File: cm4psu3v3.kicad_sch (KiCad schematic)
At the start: 26 parts, among them U13 AP64501SP-13

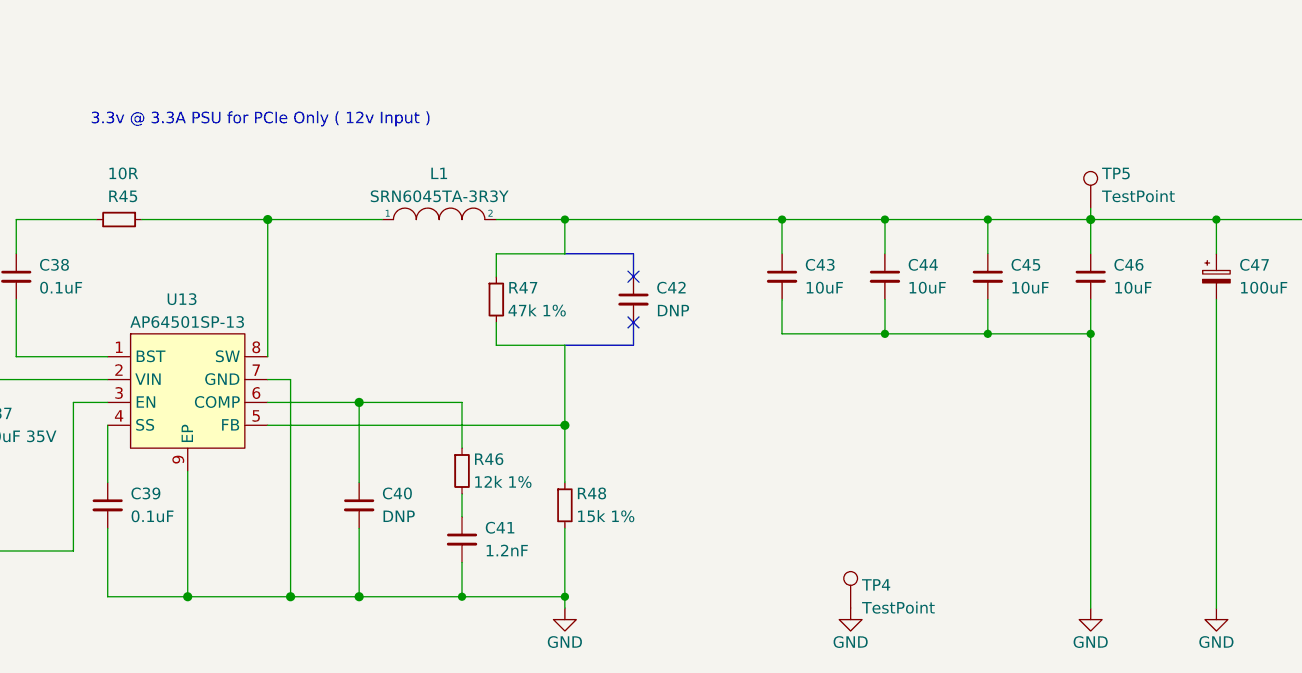
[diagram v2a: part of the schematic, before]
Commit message: added ti buffer lib
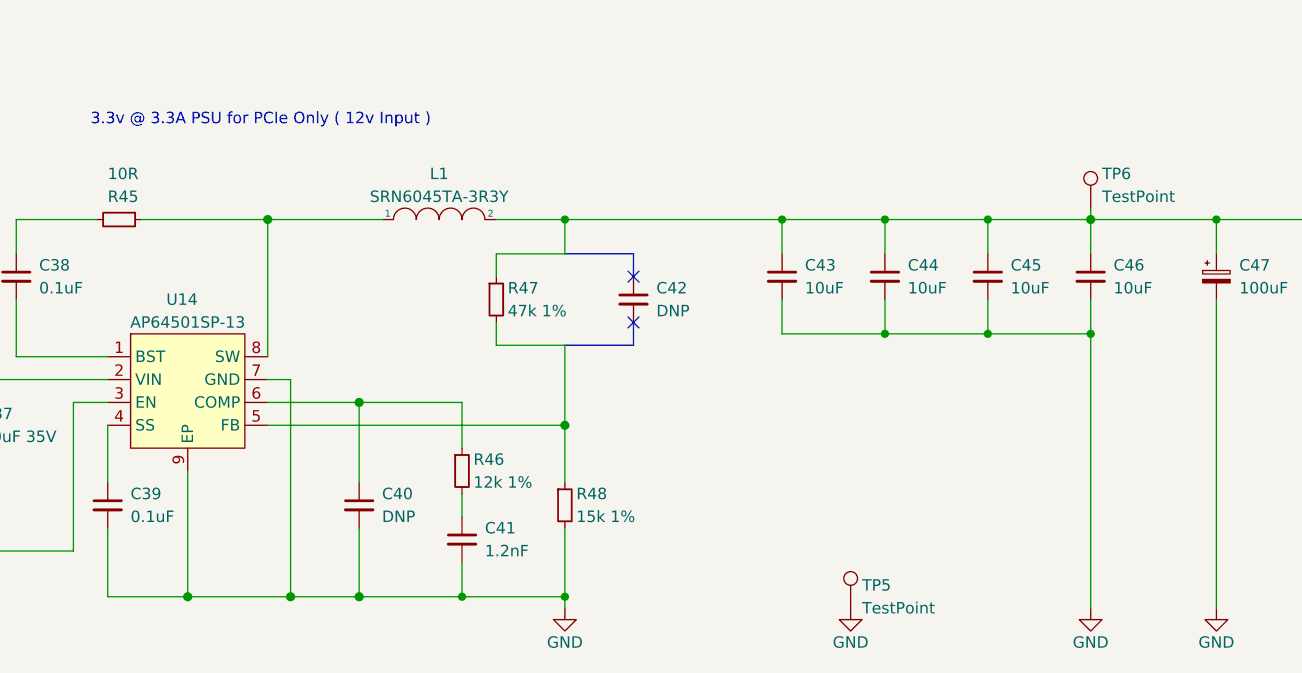
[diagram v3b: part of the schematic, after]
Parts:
- renumbered TP4 to TP5, TP5 to TP6, U13 to U14
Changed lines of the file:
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@@
   (symbol (lib_id "power:GND") (at 152.4 171.45 0) (unit 1)
     (in_bom yes) (on_board yes)
-    (property "Reference" "#PWR040" (id 0) (at 152.4 177.8 0)
+    (property "Reference" "#PWR042" (id 0) (at 152.4 177.8 0)
       (effects (font (size 1.27 1.27)) hide)
     )
@@
   (symbol (lib_id "Connector:TestPoint") (at 251.46 171.45 0) (unit 1)
     (in_bom yes) (on_board yes)
-    (property "Reference" "TP4" (id 0) (at 252.73 168.91 0)
+    (property "Reference" "TP5" (id 0) (at 252.73 168.91 0)
       (effects (font (size 1.27 1.27)) (justify left))
     )
@@
   (symbol (lib_id "power:GND") (at 292.1 171.45 0) (unit 1)
     (in_bom yes) (on_board yes)
-    (property "Reference" "#PWR044" (id 0) (at 292.1 177.8 0)
+    (property "Reference" "#PWR046" (id 0) (at 292.1 177.8 0)
       (effects (font (size 1.27 1.27)) hide)
     )
@@
   (symbol (lib_id "power:GND") (at 307.975 171.45 0) (unit 1)
     (in_bom yes) (on_board yes)
-    (property "Reference" "#PWR045" (id 0) (at 307.975 177.8 0)
+    (property "Reference" "#PWR047" (id 0) (at 307.975 177.8 0)
       (effects (font (size 1.27 1.27)) hide)
     )
@@
   (symbol (lib_id "power:GND") (at 278.13 171.45 0) (unit 1)
     (in_bom yes) (on_board yes)
-    (property "Reference" "#PWR043" (id 0) (at 278.13 177.8 0)
+    (property "Reference" "#PWR045" (id 0) (at 278.13 177.8 0)
       (effects (font (size 1.27 1.27)) hide)
     )
@@
   (symbol (lib_id "Regulator_Switching_Diodes:AP64501SP-13") (at 177.8 147.32 0) (unit 1)
     (in_bom yes) (on_board yes)
-    (property "Reference" "U13" (id 0) (at 177.165 137.16 0))
+    (property "Reference" "U14" (id 0) (at 177.165 137.16 0))
     (property "Value" "AP64501SP-13" (id 1) (at 177.8 139.7 0))
     (property "Footprint" "Regulator_Switching_Diodes:SOIC-8-1EP_3.9x4.9mm_P1.27mm_EP2.95x4.9mm_Mask2.71x3.4mm_ThermalVias" (id 2) (at 177.8 172.72 0)
@@
   (symbol (lib_id "Connector:TestPoint") (at 278.13 127 0) (unit 1)
     (in_bom yes) (on_board yes)
-    (property "Reference" "TP5" (id 0) (at 279.4 123.19 0)
+    (property "Reference" "TP6" (id 0) (at 279.4 123.19 0)
       (effects (font (size 1.27 1.27)) (justify left))
     )
@@
   (symbol (lib_id "power:GND") (at 251.46 171.45 0) (unit 1)
     (in_bom yes) (on_board yes)
-    (property "Reference" "#PWR042" (id 0) (at 251.46 177.8 0)
+    (property "Reference" "#PWR044" (id 0) (at 251.46 177.8 0)
       (effects (font (size 1.27 1.27)) hide)
     )
@@
   (symbol (lib_id "power:GND") (at 219.71 171.45 0) (unit 1)
     (in_bom yes) (on_board yes)
-    (property "Reference" "#PWR041" (id 0) (at 219.71 177.8 0)
-      (effects (font (size 1.27 1.27)) hide)
-    )
+    (property "Reference" "#PWR043" (id 0) (at 219.71 177.8 0)
+      (effects (font (size 1.27 1.27)) hide)
+    )

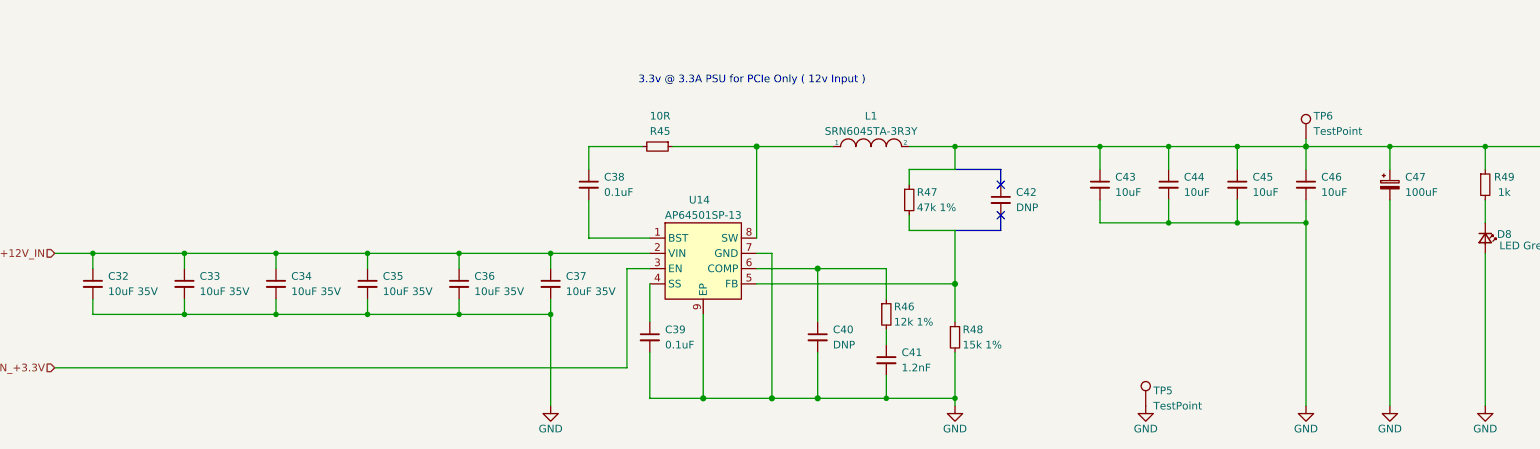
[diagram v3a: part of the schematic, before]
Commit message: initial integration of i2c arbiter
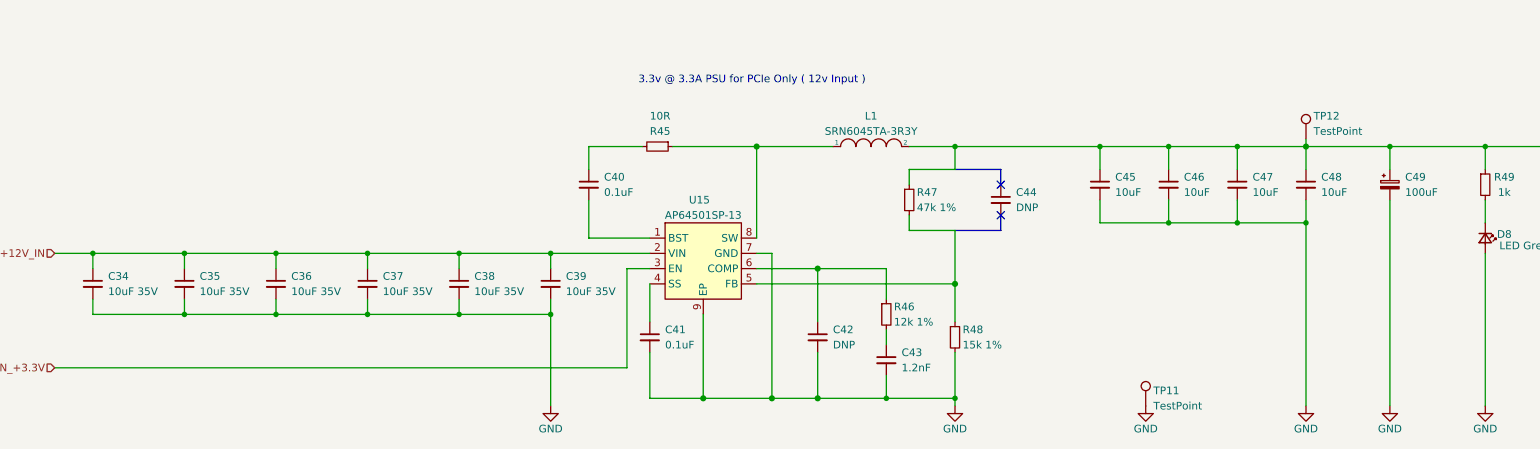
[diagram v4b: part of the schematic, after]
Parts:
- renumbered C32 to C34, C33 to C35, C34 to C36, C35 to C37, C36 to C38, C37 to C39, C38 to C40, C39 to C41, C40 to C42, C41 to C43, C42 to C44, C43 to C45, C44 to C46, C45 to C47, C46 to C48, C47 to C49, TP5 to TP11, TP6 to TP12, U14 to U15
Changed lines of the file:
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@@
   (symbol (lib_id "Device:C_Small") (at 168.91 160.02 0) (unit 1)
     (in_bom yes) (on_board yes)
-    (property "Reference" "C39" (id 0) (at 171.45 158.75 0)
+    (property "Reference" "C41" (id 0) (at 171.45 158.75 0)
       (effects (font (size 1.27 1.27)) (justify left))
     )
@@
   (symbol (lib_id "Device:C_Small") (at 121.92 151.13 0) (unit 1)
     (in_bom yes) (on_board yes)
-    (property "Reference" "C35" (id 0) (at 124.46 149.86 0)
+    (property "Reference" "C37" (id 0) (at 124.46 149.86 0)
       (effects (font (size 1.27 1.27)) (justify left))
     )
@@
   (symbol (lib_id "power:GND") (at 152.4 171.45 0) (unit 1)
     (in_bom yes) (on_board yes)
-    (property "Reference" "#PWR042" (id 0) (at 152.4 177.8 0)
+    (property "Reference" "#PWR043" (id 0) (at 152.4 177.8 0)
       (effects (font (size 1.27 1.27)) hide)
     )
@@
   (symbol (lib_id "Connector:TestPoint") (at 251.46 171.45 0) (unit 1)
     (in_bom yes) (on_board yes)
-    (property "Reference" "TP5" (id 0) (at 252.73 168.91 0)
+    (property "Reference" "TP11" (id 0) (at 252.73 168.91 0)
       (effects (font (size 1.27 1.27)) (justify left))
     )
@@
   (symbol (lib_id "Capacitor_Tantalum_SMD_MyOwn:CP_EIA-7343-31_Kemet-D") (at 292.1 134.62 0) (unit 1)
     (in_bom yes) (on_board yes)
-    (property "Reference" "C47" (id 0) (at 294.64 133.35 0)
+    (property "Reference" "C49" (id 0) (at 294.64 133.35 0)
       (effects (font (size 1.27 1.27)) (justify left))
     )
@@
   (symbol (lib_id "Device:C_Small") (at 158.75 134.62 0) (unit 1)
     (in_bom yes) (on_board yes)
-    (property "Reference" "C38" (id 0) (at 161.29 133.35 0)
+    (property "Reference" "C40" (id 0) (at 161.29 133.35 0)
       (effects (font (size 1.27 1.27)) (justify left))
     )
@@
   (symbol (lib_id "Device:C_Small") (at 243.84 134.62 0) (unit 1)
     (in_bom yes) (on_board yes)
-    (property "Reference" "C43" (id 0) (at 246.38 133.35 0)
+    (property "Reference" "C45" (id 0) (at 246.38 133.35 0)
       (effects (font (size 1.27 1.27)) (justify left))
     )
@@
   (symbol (lib_id "Device:C_Small") (at 255.27 134.62 0) (unit 1)
     (in_bom yes) (on_board yes)
-    (property "Reference" "C44" (id 0) (at 257.81 133.35 0)
+    (property "Reference" "C46" (id 0) (at 257.81 133.35 0)
       (effects (font (size 1.27 1.27)) (justify left))
     )
@@
   (symbol (lib_id "Device:C_Small") (at 278.13 134.62 0) (unit 1)
     (in_bom yes) (on_board yes)
-    (property "Reference" "C46" (id 0) (at 280.67 133.35 0)
+    (property "Reference" "C48" (id 0) (at 280.67 133.35 0)
       (effects (font (size 1.27 1.27)) (justify left))
     )
@@
   (symbol (lib_id "Device:C_Small") (at 227.33 137.16 0) (unit 1)
     (in_bom no) (on_board no)
-    (property "Reference" "C42" (id 0) (at 229.87 135.89 0)
+    (property "Reference" "C44" (id 0) (at 229.87 135.89 0)
       (effects (font (size 1.27 1.27)) (justify left))
     )
@@
   (symbol (lib_id "power:GND") (at 292.1 171.45 0) (unit 1)
     (in_bom yes) (on_board yes)
-    (property "Reference" "#PWR046" (id 0) (at 292.1 177.8 0)
+    (property "Reference" "#PWR047" (id 0) (at 292.1 177.8 0)
       (effects (font (size 1.27 1.27)) hide)
     )
@@
   (symbol (lib_id "Device:C_Small") (at 91.44 151.13 0) (unit 1)
     (in_bom yes) (on_board yes)
-    (property "Reference" "C33" (id 0) (at 93.98 149.86 0)
+    (property "Reference" "C35" (id 0) (at 93.98 149.86 0)
       (effects (font (size 1.27 1.27)) (justify left))
     )
@@
   (symbol (lib_id "Device:C_Small") (at 208.28 163.83 0) (unit 1)
     (in_bom yes) (on_board yes)
-    (property "Reference" "C41" (id 0) (at 210.82 162.56 0)
+    (property "Reference" "C43" (id 0) (at 210.82 162.56 0)
       (effects (font (size 1.27 1.27)) (justify left))
     )
@@
   (symbol (lib_id "Device:C_Small") (at 76.2 151.13 0) (unit 1)
     (in_bom yes) (on_board yes)
-    (property "Reference" "C32" (id 0) (at 78.74 149.86 0)
+    (property "Reference" "C34" (id 0) (at 78.74 149.86 0)
       (effects (font (size 1.27 1.27)) (justify left))
     )
@@
   (symbol (lib_id "power:GND") (at 307.975 171.45 0) (unit 1)
     (in_bom yes) (on_board yes)
-    (property "Reference" "#PWR047" (id 0) (at 307.975 177.8 0)
+    (property "Reference" "#PWR048" (id 0) (at 307.975 177.8 0)
       (effects (font (size 1.27 1.27)) hide)
     )
@@
   (symbol (lib_id "Device:C_Small") (at 266.7 134.62 0) (unit 1)
     (in_bom yes) (on_board yes)
-    (property "Reference" "C45" (id 0) (at 269.24 133.35 0)
+    (property "Reference" "C47" (id 0) (at 269.24 133.35 0)
       (effects (font (size 1.27 1.27)) (justify left))
     )
@@
   (symbol (lib_id "Device:C_Small") (at 137.16 151.13 0) (unit 1)
     (in_bom yes) (on_board yes)
-    (property "Reference" "C36" (id 0) (at 139.7 149.86 0)
+    (property "Reference" "C38" (id 0) (at 139.7 149.86 0)
       (effects (font (size 1.27 1.27)) (justify left))
     )
@@
   (symbol (lib_id "power:GND") (at 278.13 171.45 0) (unit 1)
     (in_bom yes) (on_board yes)
-    (property "Reference" "#PWR045" (id 0) (at 278.13 177.8 0)
+    (property "Reference" "#PWR046" (id 0) (at 278.13 177.8 0)
       (effects (font (size 1.27 1.27)) hide)
     )
@@
   (symbol (lib_id "Regulator_Switching_Diodes:AP64501SP-13") (at 177.8 147.32 0) (unit 1)
     (in_bom yes) (on_board yes)
-    (property "Reference" "U14" (id 0) (at 177.165 137.16 0))
+    (property "Reference" "U15" (id 0) (at 177.165 137.16 0))
     (property "Value" "AP64501SP-13" (id 1) (at 177.8 139.7 0))
     (property "Footprint" "Regulator_Switching_Diodes:SOIC-8-1EP_3.9x4.9mm_P1.27mm_EP2.95x4.9mm_Mask2.71x3.4mm_ThermalVias" (id 2) (at 177.8 172.72 0)
@@
   (symbol (lib_id "Device:C_Small") (at 106.68 151.13 0) (unit 1)
     (in_bom yes) (on_board yes)
-    (property "Reference" "C34" (id 0) (at 109.22 149.86 0)
+    (property "Reference" "C36" (id 0) (at 109.22 149.86 0)
       (effects (font (size 1.27 1.27)) (justify left))
     )
@@
   (symbol (lib_id "Connector:TestPoint") (at 278.13 127 0) (unit 1)
     (in_bom yes) (on_board yes)
-    (property "Reference" "TP6" (id 0) (at 279.4 123.19 0)
+    (property "Reference" "TP12" (id 0) (at 279.4 123.19 0)
       (effects (font (size 1.27 1.27)) (justify left))
     )
@@
   (symbol (lib_id "power:GND") (at 251.46 171.45 0) (unit 1)
     (in_bom yes) (on_board yes)
-    (property "Reference" "#PWR044" (id 0) (at 251.46 177.8 0)
+    (property "Reference" "#PWR045" (id 0) (at 251.46 177.8 0)
       (effects (font (size 1.27 1.27)) hide)
     )
@@
   (symbol (lib_id "Device:C_Small") (at 196.85 160.02 0) (unit 1)
     (in_bom yes) (on_board yes)
-    (property "Reference" "C40" (id 0) (at 199.39 158.75 0)
+    (property "Reference" "C42" (id 0) (at 199.39 158.75 0)
       (effects (font (size 1.27 1.27)) (justify left))
     )
@@
   (symbol (lib_id "power:GND") (at 219.71 171.45 0) (unit 1)
     (in_bom yes) (on_board yes)
-    (property "Reference" "#PWR043" (id 0) (at 219.71 177.8 0)
+    (property "Reference" "#PWR044" (id 0) (at 219.71 177.8 0)
       (effects (font (size 1.27 1.27)) hide)
     )
@@
   (symbol (lib_id "Device:C_Small") (at 152.4 151.13 0) (unit 1)
     (in_bom yes) (on_board yes)
-    (property "Reference" "C37" (id 0) (at 154.94 149.86 0)
-      (effects (font (size 1.27 1.27)) (justify left))
-    )
+    (property "Reference" "C39" (id 0) (at 154.94 149.86 0)
+      (effects (font (size 1.27 1.27)) (justify left))
+    )
